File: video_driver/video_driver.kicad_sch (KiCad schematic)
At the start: 0 parts

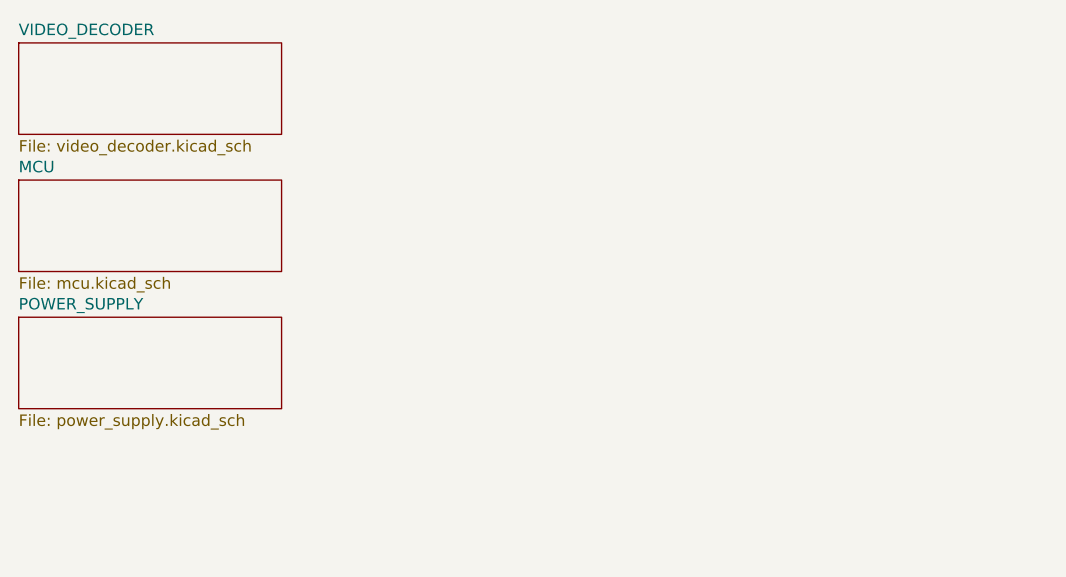
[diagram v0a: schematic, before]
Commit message: new mcu
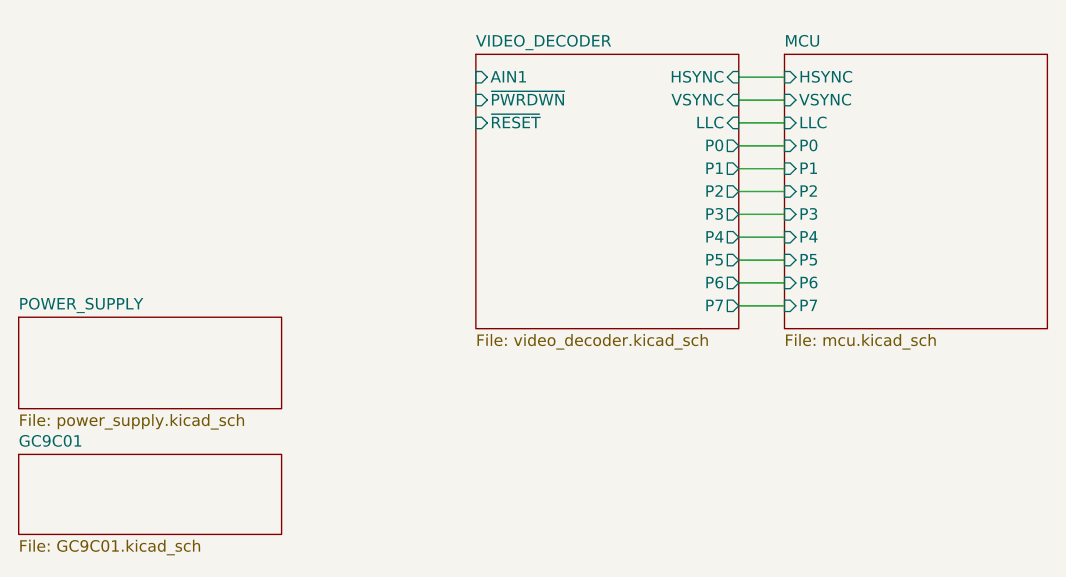
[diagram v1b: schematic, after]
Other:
- added sheet GC9C01 (GC9C01.kicad_sch)
- sheet MCU ports: added HSYNC, LLC, P0, P1, P2, P3, P4, P5, P6, P7, VSYNC; removed none
- sheet VIDEO_DECODER ports: added AIN1, HSYNC, LLC, P0, P1, P2, P3, P4, P5, P6, P7, VSYNC, ~{PWRDWN}, ~{RESET}; removed none
